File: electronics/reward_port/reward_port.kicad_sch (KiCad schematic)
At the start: 56 parts, among them J1 Conn_SWD, J2 SM10B-GHS-TB, J3 SM10B-GHS-TB, J4 SM04B-GHS-TB, J5 SM04B-GHS-TB, J6 SM02B-GHS-TB, J7 SM02B-GHS-TB, Q1 2N7002, Q2 DMG2302U, Q3 DMG2302U, Q4 DMG2302U, U1 STM32G071RBT6, U2 THVD1410DGKR, U4 THVD1410DGKR, U5 PAM8302AASCR, U6 BD6210F-E2

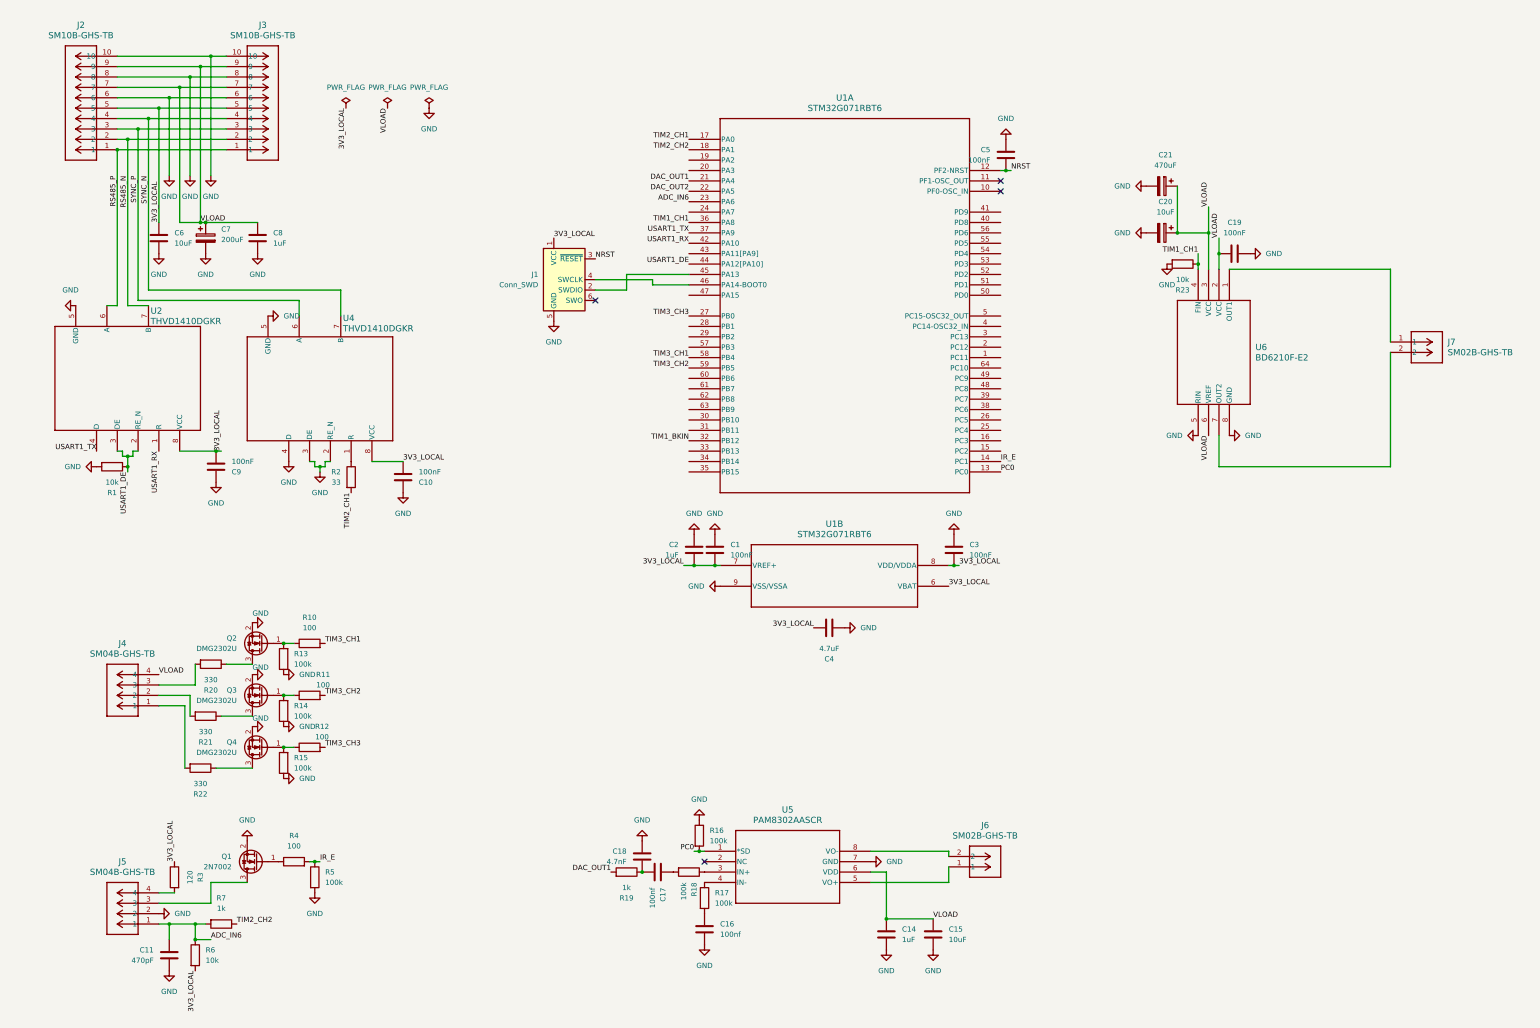
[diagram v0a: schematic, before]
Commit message: reward port pcb update
- Schematic update to smaller stm32
- Pinout update and prototype wiring guide
- PCB design (4cm x 3cm, 4 layer, components only on front side)
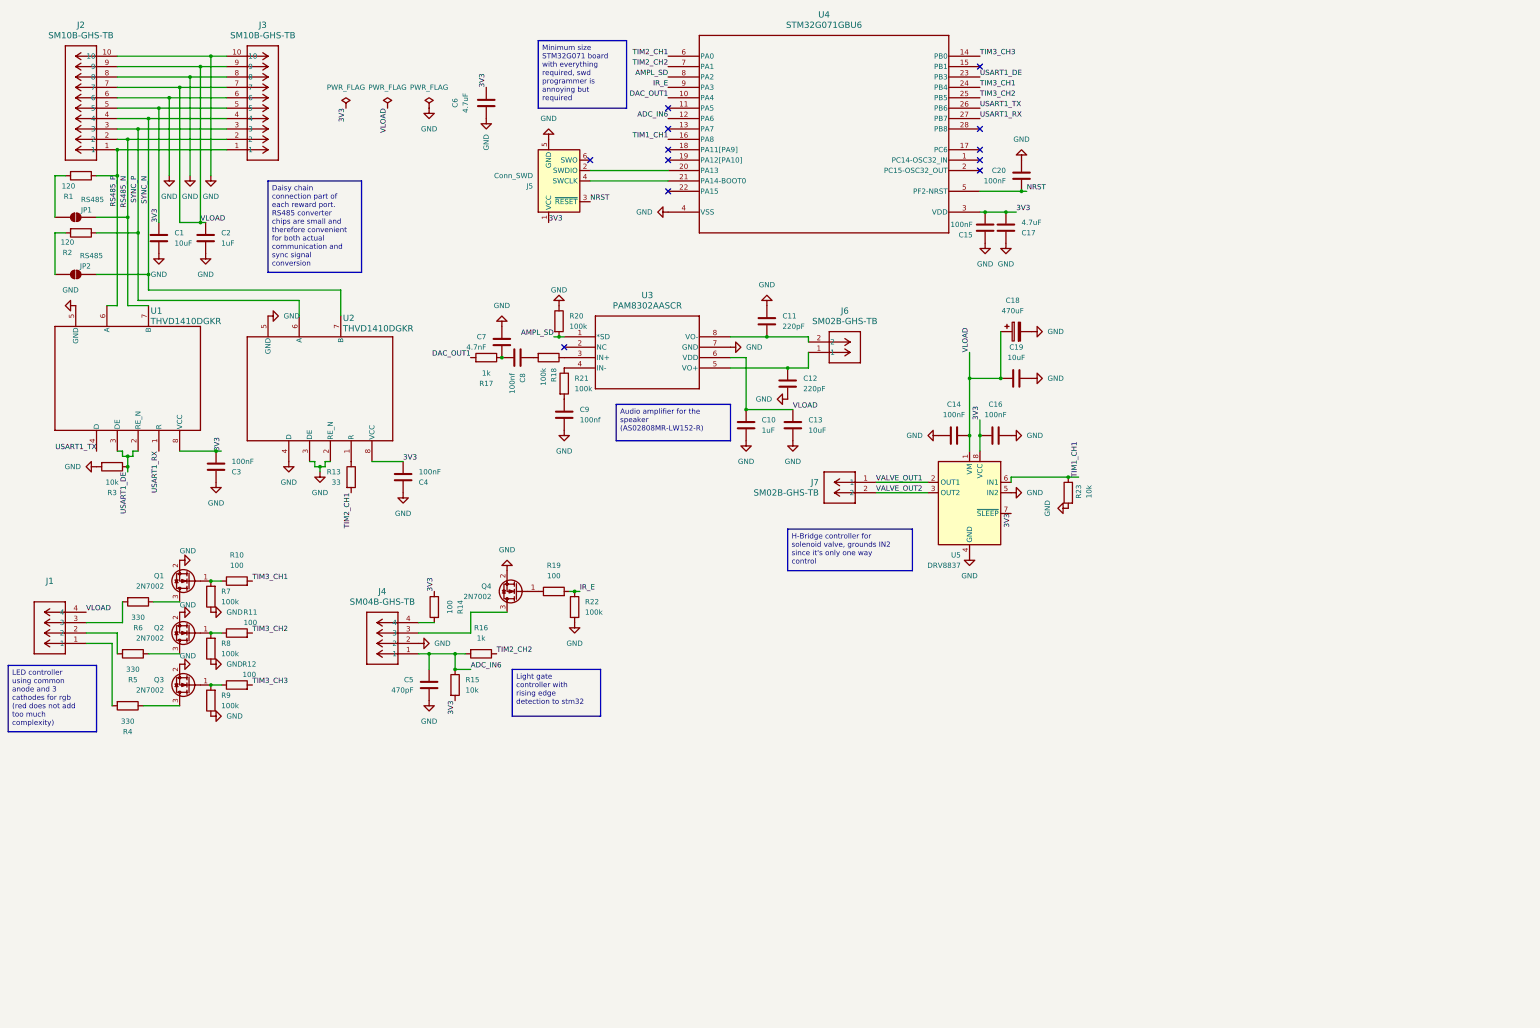
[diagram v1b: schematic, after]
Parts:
- removed C20: 10uF, symbol Device:C_Polarized
- removed C3: 100nF, symbol symbols:C
- removed C7: 200uF, symbol Device:C_Polarized
- removed Q2, Q3, Q4: DMG2302U, Package_TO_SOT_SMD:SOT-23, symbol symbols:DMG2302U
- removed U1: STM32G071RBT6, reward_port:LQFP64_10x10_STM, symbol reward_port:STM32G071RBT6
- removed U6: BD6210F-E2, SOP8_ROM, symbol reward_port:BD6210F-E2
- added C11, C12: 220pF, Capacitor_SMD:C_0402_1005Metric, symbol symbols:C
- added C14: 100nF, Capacitor_SMD:C_0402_1005Metric, symbol symbols:C
- added C19: 10uF, Capacitor_SMD:C_0603_1608Metric, symbol symbols:C
- added JP1, JP2: RS485, Jumper:SolderJumper-2_P1.3mm_Open_RoundedPad1.0x1.5mm, symbol Jumper:SolderJumper_2_Open
- added Q1, Q2, Q3: 2N7002, Package_TO_SOT_SMD:SOT-323_SC-70, symbol symbols:2N7002
- added R1, R2: 120, Resistor_SMD:R_0603_1608Metric, symbol Device:R
- added U4: STM32G071GBU6, Package_DFN_QFN:QFN-28_4x4mm_P0.5mm, symbol reward_port:STM32G071GBU6
- added U5: DRV8837, Package_SON:WSON-8-1EP_2x2mm_P0.5mm_EP0.9x1.6mm, symbol symbols:DRV8837
- C1: renamed from C6; footprint (none) -> Capacitor_SMD:C_0603_1608Metric
- C10: renamed from C14; footprint (none) -> Capacitor_SMD:C_0402_1005Metric
- C13: renamed from C15; footprint (none) -> Capacitor_SMD:C_0805_2012Metric
- C15: renamed from C1; footprint (none) -> Capacitor_SMD:C_0402_1005Metric
- C16: renamed from C19; footprint (none) -> Capacitor_SMD:C_0402_1005Metric
- C17: renamed from C2; value 1uF -> 4.7uF; footprint (none) -> Capacitor_SMD:C_0603_1608Metric
- C18: renamed from C21; footprint (none) -> Capacitor_Tantalum_SMD:CP_EIA-7360-38_Kemet-E
- C2: renamed from C8; footprint (none) -> Capacitor_SMD:C_0402_1005Metric
- C20: renamed from C5; footprint (none) -> Capacitor_SMD:C_0402_1005Metric
- C3: renamed from C9; footprint (none) -> Capacitor_SMD:C_0402_1005Metric
- C4: renamed from C10; footprint (none) -> Capacitor_SMD:C_0402_1005Metric
- C5: renamed from C11; footprint (none) -> Capacitor_SMD:C_0402_1005Metric
- C6: renamed from C4; footprint (none) -> Capacitor_SMD:C_0603_1608Metric
- C7: renamed from C18; footprint (none) -> Capacitor_SMD:C_0402_1005Metric
- C8: renamed from C17; footprint (none) -> Capacitor_SMD:C_0402_1005Metric
- C9: renamed from C16; footprint (none) -> Capacitor_SMD:C_0402_1005Metric
- J1: renamed from J4; footprint CONN_SM04B-GHS-TB_JST -> Connector_JST:JST_GH_SM04B-GHS-TB_1x04-1MP_P1.25mm_Horizontal
- J2, J3: footprint CONN_SM10B-GHS-TB_JST -> Connector_JST:JST_GH_SM10B-GHS-TB_1x10-1MP_P1.25mm_Horizontal
- J4: renamed from J5; footprint CONN_SM04B-GHS-TB_JST -> Connector_JST:JST_GH_SM04B-GHS-TB_1x04-1MP_P1.25mm_Horizontal
- J6, J7: footprint CONN_SM02B-GHS_JST -> Connector_JST:JST_GH_SM02B-GHS-TB_1x02-1MP_P1.25mm_Horizontal
- Q4: renamed from Q1; footprint Package_TO_SOT_SMD:SOT-23 -> Package_TO_SOT_SMD:SOT-323_SC-70
- R10, R11, R12, R18, R23: footprint (none) -> Resistor_SMD:R_0402_1005Metric
- R13: renamed from R2; footprint (none) -> Resistor_SMD:R_0402_1005Metric
- R14: renamed from R3; value 120 -> 100; footprint (none) -> Resistor_SMD:R_0603_1608Metric
- R15: renamed from R6; footprint (none) -> Resistor_SMD:R_0402_1005Metric
- R16: renamed from R7; footprint (none) -> Resistor_SMD:R_0402_1005Metric
- R17: renamed from R19; footprint (none) -> Resistor_SMD:R_0402_1005Metric
- R19: renamed from R4; footprint (none) -> Resistor_SMD:R_0402_1005Metric
- R20: renamed from R16; footprint (none) -> Resistor_SMD:R_0402_1005Metric
- R21: renamed from R17; footprint (none) -> Resistor_SMD:R_0402_1005Metric
- R22: renamed from R5; footprint (none) -> Resistor_SMD:R_0402_1005Metric
- R3: renamed from R1; footprint (none) -> Resistor_SMD:R_0402_1005Metric
- R4: renamed from R22; footprint (none) -> Resistor_SMD:R_0402_1005Metric
- R5: renamed from R21; footprint (none) -> Resistor_SMD:R_0402_1005Metric
- R6: renamed from R20; footprint (none) -> Resistor_SMD:R_0402_1005Metric
- R7: renamed from R13; footprint (none) -> Resistor_SMD:R_0402_1005Metric
- R8: renamed from R14; footprint (none) -> Resistor_SMD:R_0402_1005Metric
- R9: renamed from R15; footprint (none) -> Resistor_SMD:R_0402_1005Metric
- U1: renamed from U2; footprint DGK0008A_N -> Package_SO:VSSOP-8_3x3mm_P0.65mm
- U2: renamed from U4; footprint DGK0008A_N -> Package_SO:VSSOP-8_3x3mm_P0.65mm
- U3: renamed from U5; footprint PAM8302AASCR_DIO -> reward_port:PAM8302AASCR_DIO
- renumbered J1 to J5
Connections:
- net ADC_IN6: now also U4.12 (PA6)
- net DAC_OUT1: now also U4.10 (PA4)
- net GND: now also C11.1, C12.1, C14.2, C19.2, Q1.2 (S), Q2.2 (S), Q3.2 (S), U4.4 (VSS), U5.4 (GND), U5.5 (IN2), U5.9 (GND)
- net IR_E: now also U4.9 (PA3)
- net NRST: now also U4.5 (PF2-NRST)
- net RS485_N: now also JP1.2 (B)
- net RS485_P: now also R1.1
- net SYNC_N: now also JP2.2 (B)
- net SYNC_P: now also R2.1
- net TIM1_CH1: now also U4.16 (PA8), U5.6 (IN1)
- net TIM2_CH1: now also U4.6 (PA0)
- net TIM2_CH2: now also U4.7 (PA1)
- net TIM3_CH1: now also U4.24 (PB4)
- net TIM3_CH2: now also U4.25 (PB5)
- net TIM3_CH3: now also U4.14 (PB0)
- net USART1_DE: now also U4.23 (PB3)
- net USART1_RX: now also U4.27 (PB7)
- net USART1_TX: now also U4.26 (PB6)
- net VLOAD: now also C14.1, C19.1, U5.1 (VM); no longer C16.1
- net at J6.1, U3.5 (VO+): now also C12.2
- net at J6.2, U3.8 (VO-): now also C11.2
- net at R11.1, R8.2: now also Q2.1 (G)
- net at R5.1: now also Q2.3 (D)
- net at J5.2 (SWDIO): now also U4.20 (PA13)
- net at J5.4 (SWCLK): now also U4.21 (PA14-BOOT0)
- net at R10.1, R7.2: now also Q1.1 (G)
- net at R6.1: now also Q1.3 (D)
- net at R4.1: now also Q3.3 (D)
- net VALVE_OUT1: now reaches J7.1
- net VALVE_OUT1: now also U5.2 (OUT1)
- net VALVE_OUT2: now reaches J7.2
- net VALVE_OUT2: now also U5.3 (OUT2)
- net at R12.1, R9.2: now also Q3.1 (G)
- net 3V3_LOCAL renamed 3V3
- net 3V3: now also C16.1, U4.3 (VDD), U5.7 (~{SLEEP}), U5.8 (VCC)
- net PC0 renamed AMPL_SD
- net AMPL_SD: now also U4.8 (PA2)
- new net: JP2.1 (A), R2.2
- new net: JP1.1 (A), R1.2
- no-connect marks 4 -> 12
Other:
- moved on the sheet: C10, C13, C15, C16, C17, C18, C2, C20, C5, C6, C7, C8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

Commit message: small update to exact bulk capacitor, peripheral order list
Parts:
- C18: footprint Capacitor_Tantalum_SMD:CP_EIA-7360-38_Kemet-E -> Capacitor_Tantalum_SMD:CP_EIA-7343-43_Kemet-X
- J2, J3: footprint Connector_JST:JST_GH_SM10B-GHS-TB_1x10-1MP_P1.25mm_Horizontal -> Connector_JST:JST_PH_S10B-PH-SM4-TB_1x10-1MP_P2.00mm_Horizontal
- Q1, Q2, Q3, Q4: value 2N7002 -> 2N7002PW
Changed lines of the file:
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@@
 		)
 	)
+	(text_box "Ordered with SN65HVD75DGKR due to availability"
+		(exclude_from_sim no)
+		(at 69.85 132.9324 0)
+		(size 22.86 8.0376)
+		(margins 0.9525 0.9525 0.9525 0.9525)
+		(stroke
+			(width 0)
+			(type solid)
+		)
+		(fill
+			(type none)
+		)
+		(effects
+			(font
+				(size 1.27 1.27)
+			)
+			(justify left top)
+		)
+	)
 	(text_box "LED controller using common anode and 3 cathodes for rgb (red does not add too much complexity)"
 		(exclude_from_sim no)
@@
 			)
 		)
-		(property "Footprint" "Capacitor_Tantalum_SMD:CP_EIA-7360-38_Kemet-E"
+		(property "Footprint" "Capacitor_Tantalum_SMD:CP_EIA-7343-43_Kemet-X"
 			(at 265.43 92.4052 0)
 			(hide yes)
@@
 			)
 		)
-		(property "Value" "2N7002"
+		(property "Value" "2N7002PW"
 			(at 53.34 166.3699 0)
 			(show_name no)
@@
 			)
 		)
-		(property "Value" "2N7002"
+		(property "Value" "2N7002PW"
 			(at 53.34 179.0699 0)
 			(show_name no)
@@
 			)
 		)
-		(property "Footprint" "Connector_JST:JST_GH_SM10B-GHS-TB_1x10-1MP_P1.25mm_Horizontal"
+		(property "Footprint" "Connector_JST:JST_PH_S10B-PH-SM4-TB_1x10-1MP_P2.00mm_Horizontal"
 			(at 68.58 46.99 0)
 			(hide yes)
@@
 			)
 		)
-		(property "Value" "2N7002"
+		(property "Value" "2N7002PW"
 			(at 53.34 153.6699 0)
 			(show_name no)
@@
 		(in_pos_files yes)
 		(dnp no)
-		(fields_autoplaced yes)
 		(property "Reference" "J2"
 			(at 33.02 16.51 0)
@@
 			)
 		)
-		(property "Footprint" "Connector_JST:JST_GH_SM10B-GHS-TB_1x10-1MP_P1.25mm_Horizontal"
+		(property "Footprint" "Connector_JST:JST_PH_S10B-PH-SM4-TB_1x10-1MP_P2.00mm_Horizontal"
 			(at 41.91 46.99 0)
 			(hide yes)
@@
 		)
 		(property "Datasheet" "SM10B-GHS-TB"
-			(at 41.91 46.99 0)
+			(at 35.052 50.8 0)
 			(hide yes)
 			(show_name no)
@@
 			)
 		)
-		(property "Value" "2N7002"
+		(property "Value" "2N7002PW"
 			(at 133.35 156.2099 0)
 			(show_name no)
